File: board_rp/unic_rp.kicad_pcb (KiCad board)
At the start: 4 copper layers, 50 x 15.2 mm, 210 parts, among them J2 USB_C_Receptacle, Q1 2N7002, Q10 2N7002, Q11 2N7002, Q12 2N7002, Q13 2N7002, Q14 2N7002, Q15 2N7002, Q16 2N7002, Q17 2N7002, Q18 2N7002, Q19 2N7002, Q2 2N7002, Q20 2N7002, Q21 2N7002, Q22 2N7002, Q23 2N7002, Q24 2N7002, Q25 2N7002, Q26 2N7002, Q27 2N7002, Q28 2N7002, Q29 2N7002, Q3 2N7002, Q30 2N7002, Q31 2N7002, Q32 2N7002, Q33 2N7002, Q34 2N7002, Q35 2N7002, Q36 2N7002, Q37 2N7002, Q38 2N7002, Q39 2N7002, Q4 2N7002, Q40 2N7002, Q41 2N7002, Q42 AO3401A, Q43 2N7002, Q5 2N7002, Q6 2N7002, Q7 2N7002, Q8 2N7002, Q9 2N7002, U1 RP2350_80QFN, U10 ESD224DQA, U12 4066, U2 ESD224DQA, U3 MIC5203-3.3BM5, U4 APS6404L-3SQR-ZR, U6 TPS562242DRLR, U7 W25Q16JVUXIQ, U8 LM393, Y1 12MHz

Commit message: Work towards power routing
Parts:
- moved R1 12.8 mm to (54.9, 57.6)
- moved FID8 0.40 mm to (56.9, 57.5)
- moved LED_DONE1 0.40 mm to (40.3, 57.5)
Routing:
- net LINE: track 37.9 -> 135.8 mm, vias 17 -> 23
- net +3V3: track 42.2 -> 136.7 mm, vias 20 -> 23
- net +5V: track 70.2 -> 128.9 mm, vias 17 -> 19
- net GND: track 61.3 -> 89.6 mm, vias 31 -> 44
- net +1V1: track 15.4 -> 34.1 mm
- net /LED_OUT: track 22.5 -> 8.57 mm, vias 2 -> 0
- net Net-(LED_DONE1-A): track 1.02 -> 14.3 mm
- net /SPI_CLK: track 49.2 -> 57.5 mm
- net Net-(R24-Pad2): track 29.0 -> 31.7 mm
- net /SWCLK: track 32.7 -> 35.3 mm
- net /SWD: track 33.1 -> 35.1 mm
- net /PIN30: track 24.3 -> 25.9 mm
- net /PIN28_F: track 25.9 -> 24.3 mm
- net /USB_TXP: track 22.2 -> 23.6 mm, vias 4 -> 3
- net /FLASH_CS_N: track 36.6 -> 38.0 mm
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- removed copper zone on In2.Cu, net +1V1
- removed copper zone on In2.Cu, net +3V3
- removed copper zone on In2.Cu, net +5V
- removed copper zone on In2.Cu, net LINE

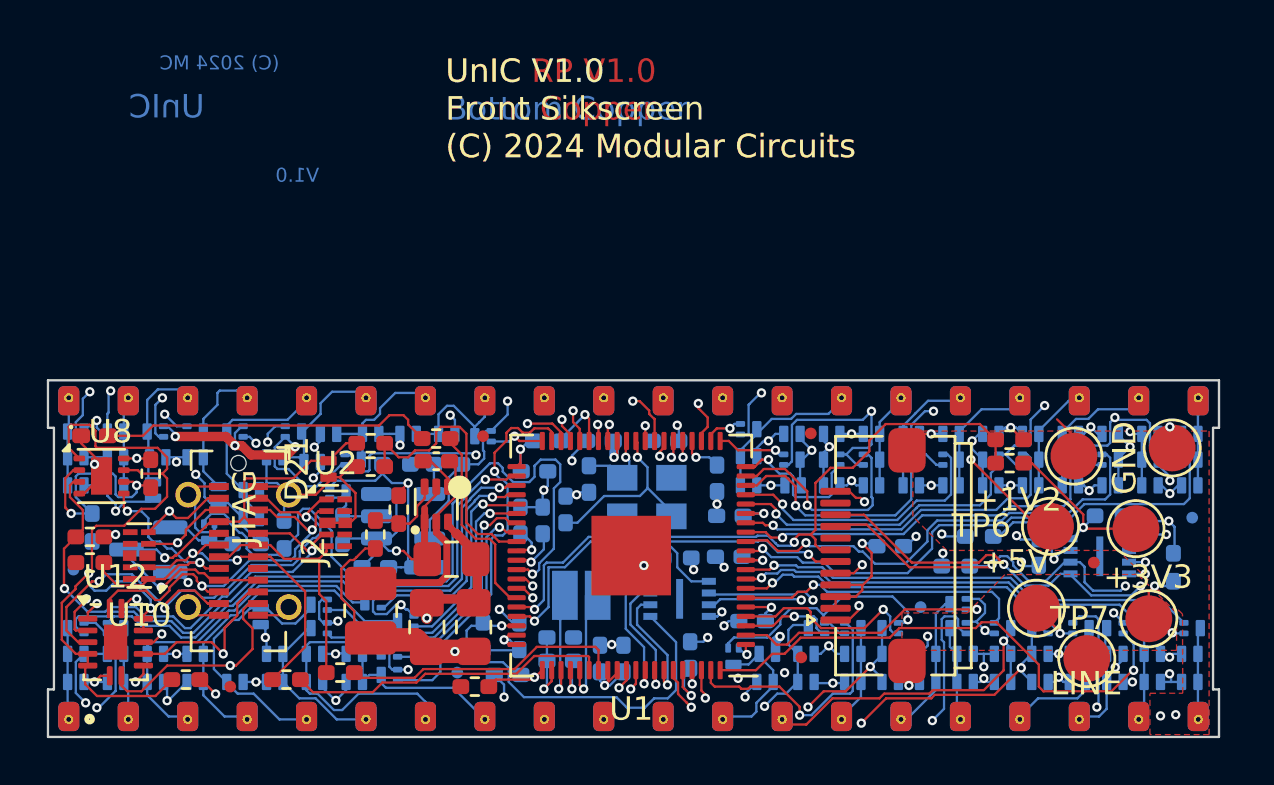
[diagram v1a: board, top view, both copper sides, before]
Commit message: More or less complete routing.
There are a few clearance violations with NPTH that doesn't
make sense. Also, power planes are not in yet, only wires.
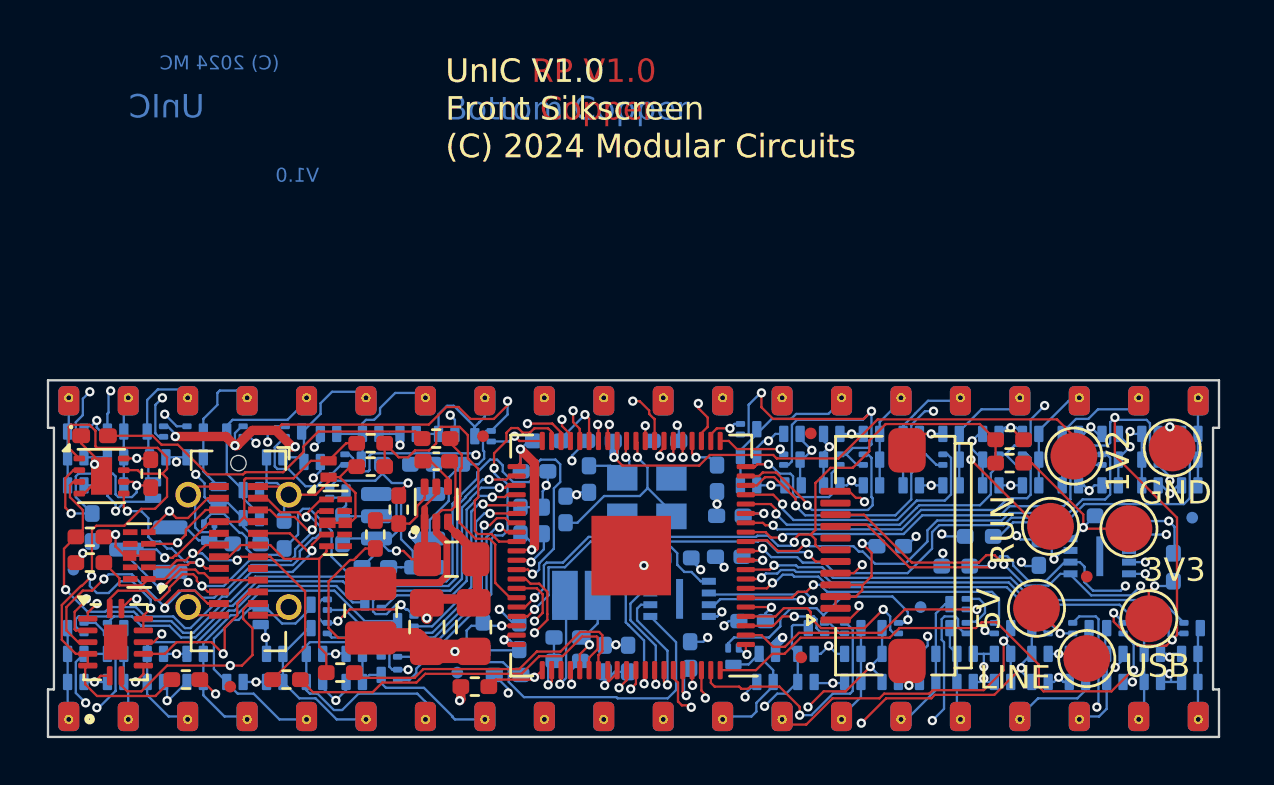
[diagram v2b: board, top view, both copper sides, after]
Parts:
- moved FID6 0.67 mm to (82.7, 63.5)
- moved C12 0.30 mm to (60.5, 66.1)
- moved C26 0.30 mm to (60.5, 67.1)
- moved TP3 0.30 mm to (84.5, 61.4)
- moved C13 0.20 mm to (63.1, 67.0)
- moved C9 0.20 mm to (62.1, 67.0)
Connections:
- net Net-(R21-Pad1) renamed /USB_BOOT
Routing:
- net +5V: track 128.9 -> 189.4 mm, vias 19 -> 20
- net +3V3: track 136.7 -> 157.4 mm, vias 23 -> 21
- net LINE: track 135.8 -> 154.8 mm
- net +1V1: track 34.1 -> 50.6 mm
- net GND: track 89.6 -> 103.3 mm, vias 44 -> 45
- net /VREG_AVDD: track 13.1 -> 3.20 mm, vias 2 -> 1
- net Net-(U1-USB_DM): track 13.8 -> 15.5 mm
- net Net-(U1-USB_DP): track 12.0 -> 13.1 mm
- net /UART_TX: track 24.2 -> 25.3 mm
- net /UART_RX: track 22.8 -> 23.7 mm
- net Net-(LED_DONE1-A): track 14.3 -> 15.1 mm
- net /PIN8_F: track 16.7 -> 16.2 mm
- removed copper zone on F.Cu, net +3V3
- removed copper zone on In1.Cu, net +3V3
- removed copper zone on F.Cu, net +5V
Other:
- board text added: "1V2"
- board text added: "3V3"
- board text added: "5V"
- board text added: "RUN"
- board text added: "USB"
- board text removed: "+1V2"
- board text removed: "+3V3"
- board text removed: "+5V"
- board text removed: "JTAG"

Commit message: Much UnIC RP cleanup.
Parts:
- moved R16 1.43 mm to (45.5, 62.7), turned to 90 degrees
- moved Q43 0.51 mm to (45.3, 61.1), turned to 180 degrees
- moved D81 0.20 mm to (45.6, 59.8)
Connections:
- U12 pad 10: /USB_RXM -> /USB_RXP
- U12 pad 11: /UART_TX -> /UART_RX
- U12 pad 8: /USB_RXP -> /USB_RXM
- U12 pad 9: /UART_RX -> /UART_TX
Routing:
- net /USB_RXM: track 17.0 -> 27.2 mm
- net /UART_RX: track 23.7 -> 27.1 mm
- net /USB_DM: track 13.4 -> 16.0 mm
- net /SPI_MOSI_IO0: track 57.5 -> 56.1 mm
- net /USB_CC2: track 11.4 -> 10.1 mm
- net /USB_CC1: track 22.2 -> 23.5 mm
- net LINE: track 154.8 -> 156.0 mm
- net /USB_PWR_EN: track 31.6 -> 30.4 mm
- net /UART_TX: track 25.3 -> 24.2 mm
- net /USB_RXP: track 22.1 -> 23.1 mm
- net +1V1: track 50.6 -> 51.6 mm
- net /USB_TXP: track 23.6 -> 22.5 mm
- net +5V: track 189.4 -> 190.4 mm
- net /PIN30: track 25.9 -> 25.1 mm
- net /VBUS: track 20.5 -> 21.3 mm
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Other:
- board text removed: "(C) 2024 MC"
- board text removed: "UnIC"
- board text removed: "UnIC RP V1.0 Front Copper (C) 2024 Modular Circuits"
- board text removed: "UnIC V1.0 Bottom Copper (C) 2024 Modular Circuits"
- board text removed: "UnIC V1.0 Front Silkscreen (C) 2024 Modular Circuits"
- board text removed: "UnIC V1.0 Layer 2 Copper (C) 2024 Modular Circuits"
- board text removed: "UnIC V1.0 Layer 3 Copper (C) 2024 Modular Circuits"
- board text removed: "V1.0"
